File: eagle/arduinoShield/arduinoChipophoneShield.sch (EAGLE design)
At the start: 29 parts

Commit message: Updated to R1.2, which fixes the missing Pin on the screen header. Also has CS connected now too
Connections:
- net 5V: now also SCREEN_NUMPAD.9; no longer SCREEN_NUMPAD.8
- net A0: now also SCREEN_NUMPAD.11; no longer SCREEN_NUMPAD.10
- net A1: now also SCREEN_NUMPAD.12; no longer SCREEN_NUMPAD.11
- net A2: now also SCREEN_NUMPAD.13; no longer SCREEN_NUMPAD.12
- net A3: now also SCREEN_NUMPAD.14; no longer SCREEN_NUMPAD.13
- net A4: now also SCREEN_NUMPAD.15; no longer SCREEN_NUMPAD.14
- net A5: now also SCREEN_NUMPAD.16; no longer SCREEN_NUMPAD.15
- net A6: now also SCREEN_NUMPAD.17; no longer SCREEN_NUMPAD.16
- net A7: now also SCREEN_NUMPAD.18; no longer SCREEN_NUMPAD.17
- net A8: no longer SCREEN_NUMPAD.18
- net D48: now also SCREEN_NUMPAD.6
- net D49: now also SCREEN_NUMPAD.7
- net GND: now also SCREEN_NUMPAD.10; no longer SCREEN_NUMPAD.6, SCREEN_NUMPAD.9
- net RES: now also SCREEN_NUMPAD.8; no longer SCREEN_NUMPAD.7
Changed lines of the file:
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@@
 </segment>
 <segment>
-<pinref part="SCREEN_NUMPAD" gate="G$1" pin="7"/>
-<wire x1="175.26" y1="134.62" x2="172.72" y2="134.62" width="0.1524" layer="91"/>
+<pinref part="SCREEN_NUMPAD" gate="G$1" pin="8"/>
+<wire x1="190.5" y1="134.62" x2="193.04" y2="134.62" width="0.1524" layer="91"/>
 </segment>
 </net>
@@
 </segment>
 <segment>
-<pinref part="SCREEN_NUMPAD" gate="G$1" pin="8"/>
-<wire x1="190.5" y1="134.62" x2="193.04" y2="134.62" width="0.1524" layer="91"/>
-</segment>
-<segment>
 <pinref part="OK1" gate="G$1" pin="VCC"/>
 <wire x1="137.16" y1="55.88" x2="137.16" y2="68.58" width="0.1524" layer="91"/>
@@
 <pinref part="SV3" gate="G$1" pin="1"/>
 <wire x1="30.48" y1="83.82" x2="25.4" y2="83.82" width="0.1524" layer="91"/>
+</segment>
+<segment>
+<pinref part="SCREEN_NUMPAD" gate="G$1" pin="9"/>
+<wire x1="175.26" y1="132.08" x2="172.72" y2="132.08" width="0.1524" layer="91"/>
 </segment>
 </net>
@@
 </segment>
 <segment>
-<pinref part="SCREEN_NUMPAD" gate="G$1" pin="6"/>
-<wire x1="190.5" y1="137.16" x2="193.04" y2="137.16" width="0.1524" layer="91"/>
-</segment>
-<segment>
-<pinref part="SCREEN_NUMPAD" gate="G$1" pin="9"/>
-<wire x1="175.26" y1="132.08" x2="172.72" y2="132.08" width="0.1524" layer="91"/>
-</segment>
-<segment>
 <pinref part="MIDI_OUT" gate="G$1" pin="2"/>
 <wire x1="86.36" y1="81.28" x2="101.6" y2="81.28" width="0.1524" layer="91"/>
@@
 <pinref part="GND16" gate="1" pin="GND"/>
 </segment>
+<segment>
+<pinref part="SCREEN_NUMPAD" gate="G$1" pin="10"/>
+<wire x1="190.5" y1="132.08" x2="193.04" y2="132.08" width="0.1524" layer="91"/>
+</segment>
 </net>
 <net name="VIN" class="0">
@@
 </segment>
 <segment>
-<pinref part="SCREEN_NUMPAD" gate="G$1" pin="10"/>
-<wire x1="190.5" y1="132.08" x2="193.04" y2="132.08" width="0.1524" layer="91"/>
+<pinref part="SCREEN_NUMPAD" gate="G$1" pin="11"/>
+<wire x1="175.26" y1="129.54" x2="172.72" y2="129.54" width="0.1524" layer="91"/>
 </segment>
 </net>
@@
 </segment>
 <segment>
-<pinref part="SCREEN_NUMPAD" gate="G$1" pin="11"/>
-<wire x1="175.26" y1="129.54" x2="172.72" y2="129.54" width="0.1524" layer="91"/>
+<pinref part="SCREEN_NUMPAD" gate="G$1" pin="12"/>
+<wire x1="190.5" y1="129.54" x2="193.04" y2="129.54" width="0.1524" layer="91"/>
 </segment>
 </net>
@@
 </segment>
 <segment>
-<pinref part="SCREEN_NUMPAD" gate="G$1" pin="12"/>
-<wire x1="190.5" y1="129.54" x2="193.04" y2="129.54" width="0.1524" layer="91"/>
+<pinref part="SCREEN_NUMPAD" gate="G$1" pin="13"/>
+<wire x1="175.26" y1="127" x2="172.72" y2="127" width="0.1524" layer="91"/>
 </segment>
 </net>
@@
 </segment>
 <segment>
-<pinref part="SCREEN_NUMPAD" gate="G$1" pin="13"/>
-<wire x1="175.26" y1="127" x2="172.72" y2="127" width="0.1524" layer="91"/>
+<pinref part="SCREEN_NUMPAD" gate="G$1" pin="14"/>
+<wire x1="190.5" y1="127" x2="193.04" y2="127" width="0.1524" layer="91"/>
 </segment>
 </net>
@@
 </segment>
 <segment>
-<pinref part="SCREEN_NUMPAD" gate="G$1" pin="14"/>
-<wire x1="190.5" y1="127" x2="193.04" y2="127" width="0.1524" layer="91"/>
+<pinref part="SCREEN_NUMPAD" gate="G$1" pin="15"/>
+<wire x1="175.26" y1="124.46" x2="172.72" y2="124.46" width="0.1524" layer="91"/>
 </segment>
 </net>
@@
 </segment>
 <segment>
-<pinref part="SCREEN_NUMPAD" gate="G$1" pin="15"/>
-<wire x1="175.26" y1="124.46" x2="172.72" y2="124.46" width="0.1524" layer="91"/>
+<pinref part="SCREEN_NUMPAD" gate="G$1" pin="16"/>
+<wire x1="190.5" y1="124.46" x2="193.04" y2="124.46" width="0.1524" layer="91"/>
 </segment>
 </net>
@@
 </segment>
 <segment>
-<pinref part="SCREEN_NUMPAD" gate="G$1" pin="16"/>
-<wire x1="190.5" y1="124.46" x2="193.04" y2="124.46" width="0.1524" layer="91"/>
+<pinref part="SCREEN_NUMPAD" gate="G$1" pin="17"/>
+<wire x1="175.26" y1="121.92" x2="172.72" y2="121.92" width="0.1524" layer="91"/>
 </segment>
 </net>
@@
 </segment>
 <segment>
-<pinref part="SCREEN_NUMPAD" gate="G$1" pin="17"/>
-<wire x1="175.26" y1="121.92" x2="172.72" y2="121.92" width="0.1524" layer="91"/>
+<pinref part="SCREEN_NUMPAD" gate="G$1" pin="18"/>
+<wire x1="190.5" y1="121.92" x2="193.04" y2="121.92" width="0.1524" layer="91"/>
 </segment>
 </net>
@@
 <label x="175.26" y="88.9" size="1.778" layer="95" rot="R90"/>
 <pinref part="JP2" gate="1" pin="1"/>
-</segment>
-<segment>
-<pinref part="SCREEN_NUMPAD" gate="G$1" pin="18"/>
-<wire x1="190.5" y1="121.92" x2="193.04" y2="121.92" width="0.1524" layer="91"/>
 </segment>
 </net>
@@
 <pinref part="SV1" gate="G$1" pin="27"/>
 </segment>
+<segment>
+<pinref part="SCREEN_NUMPAD" gate="G$1" pin="6"/>
+<wire x1="190.5" y1="137.16" x2="193.04" y2="137.16" width="0.1524" layer="91"/>
+</segment>
 </net>
 <net name="D50" class="0">
@@
 <pinref part="SV1" gate="G$1" pin="28"/>
 </segment>
-</net>
+<segment>
+<pinref part="SCREEN_NUMPAD" gate="G$1" pin="7"/>
+<wire x1="175.26" y1="134.62" x2="172.72" y2="134.62" width="0.1524" layer="91"/>
+</segment>
+</net>

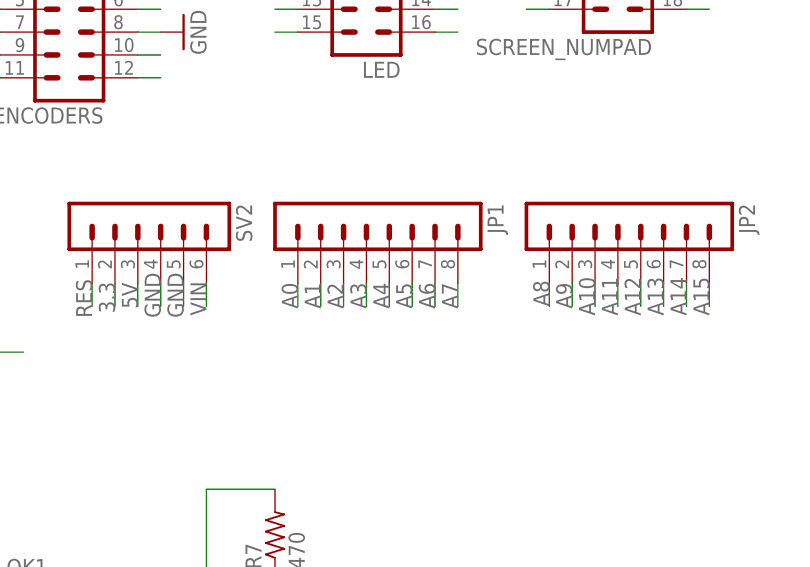
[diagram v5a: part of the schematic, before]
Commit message: Updated to R1.2, which fixes the missing Pin on the screen header. Also has CS connected now too
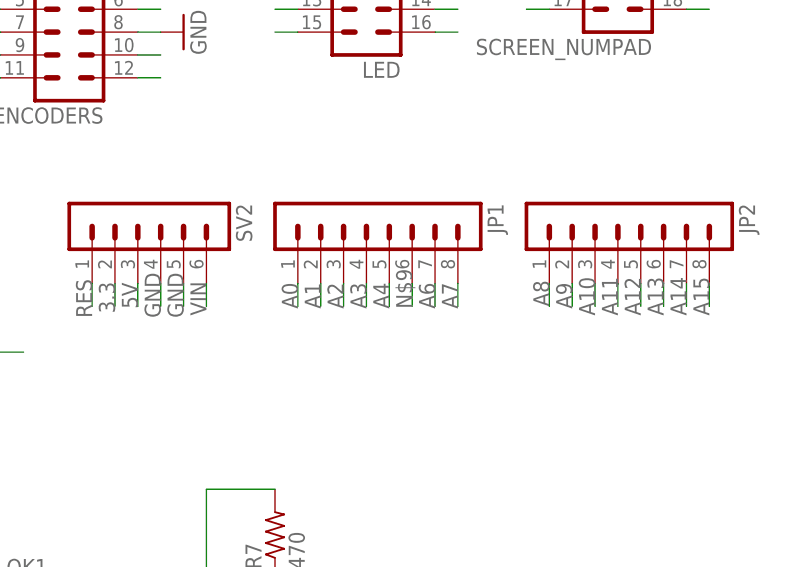
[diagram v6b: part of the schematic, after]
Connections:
- net A5 renamed N$9
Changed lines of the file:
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@@
 </segment>
 </net>
-<net name="A5" class="0">
+<net name="N$9" class="0">
 <segment>
 <wire x1="160.02" y1="88.9" x2="160.02" y2="91.44" width="0.1524" layer="91"/>

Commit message: Updated to R1.3, correct RX/TX pins. Not that I'm going to reprint it, but for good measure...
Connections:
- net D18: now also MIDI_OUT.5
- net D19: now also OK1.VO, R7.1
- net RX0: no longer OK1.VO, R7.1
- net TX1: no longer MIDI_OUT.5
